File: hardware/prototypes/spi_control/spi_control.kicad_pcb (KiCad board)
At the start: 4 copper layers, 66.9 x 43.2 mm, 87 parts, among them J1 USB_B_Micro, J39 Versa_1, J40 Versa_2, U1 ST1L08SPU33R, U2 MCP2210-I_MQ, U3 ADAR7251, U4 BGT24_Module, Y1 12MHZ, Y2 40MHz

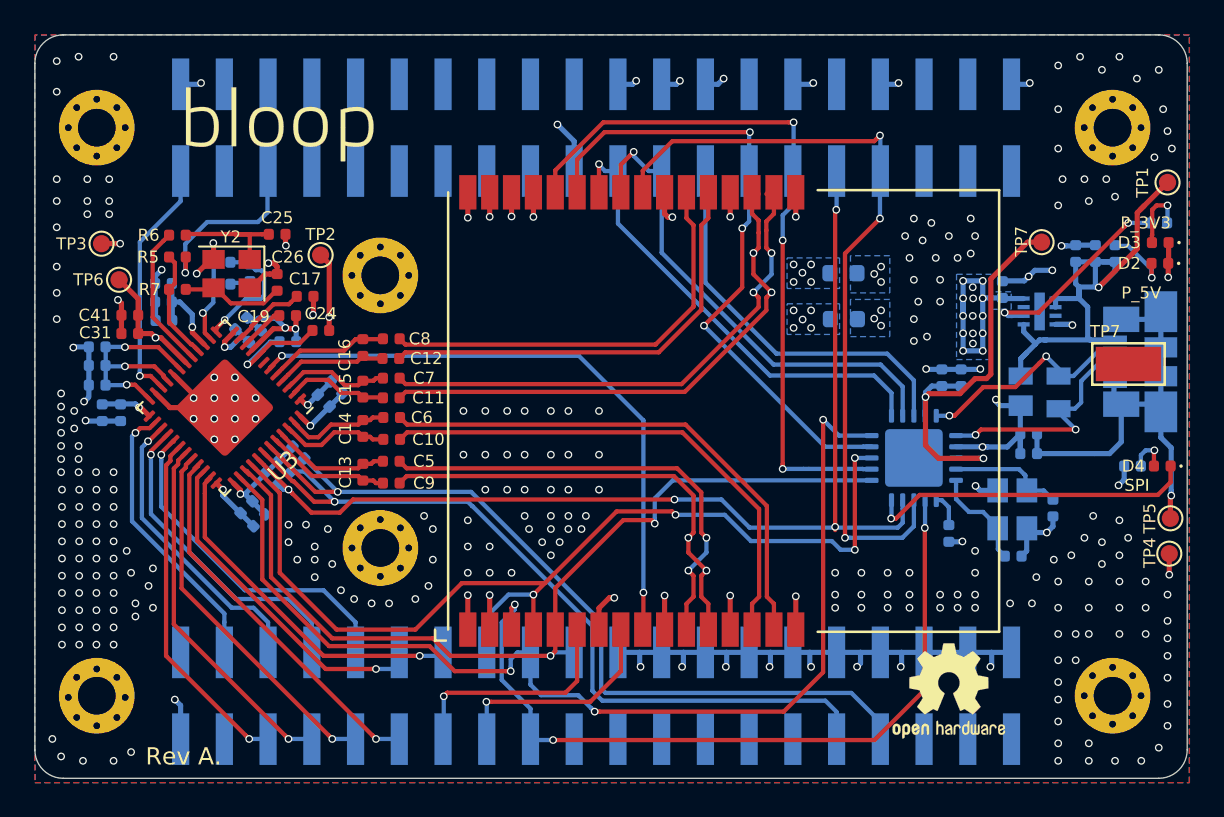
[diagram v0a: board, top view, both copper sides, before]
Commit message: Moved keystone to satisfy Leo.
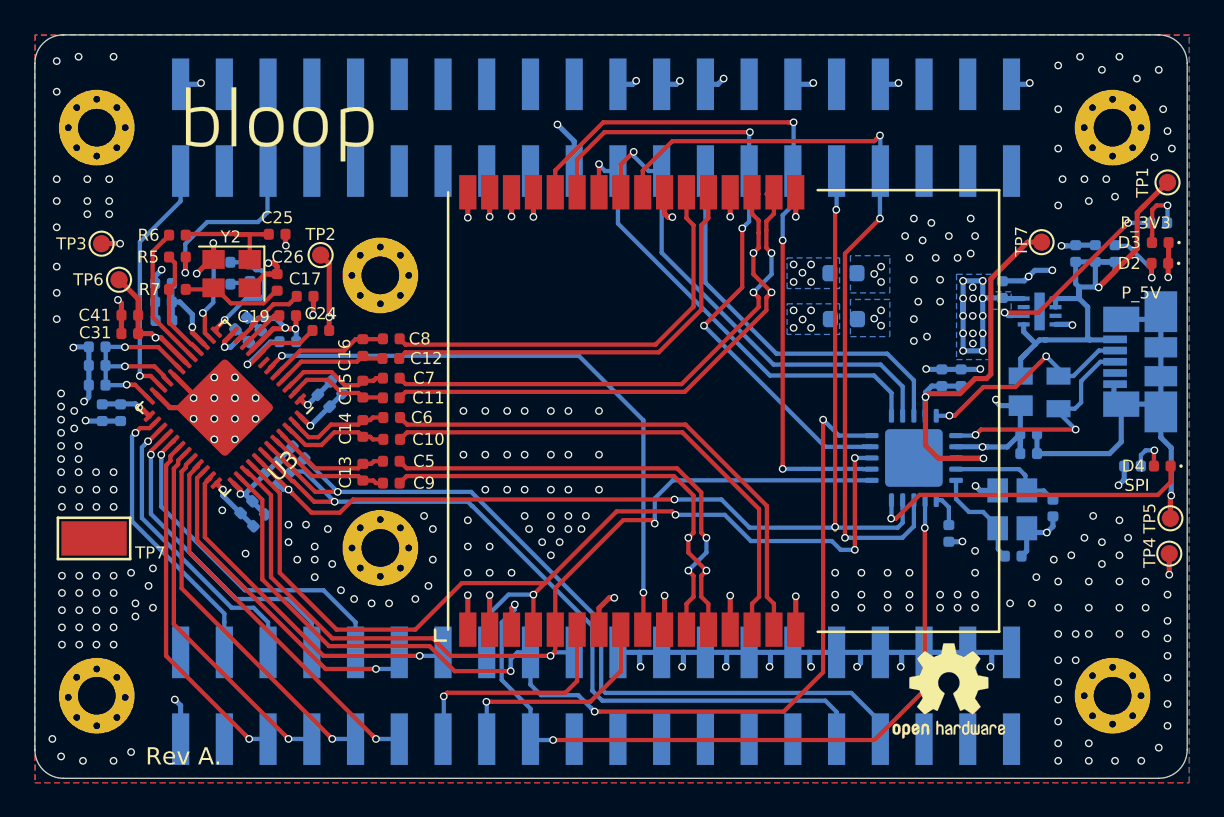
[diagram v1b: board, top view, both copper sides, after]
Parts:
- moved TP7 60.9 mm to (116.7, 114.3)
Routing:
- net GND: vias 261 -> 250
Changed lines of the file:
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@@
     (thickness 1.6)
     (drawings 15)
-    (tracks 1359)
+    (tracks 1348)
     (zones 0)
     (modules 87)
@@
   )
   (module TestPoint:TestPoint_Keystone_5019_Minature (layer F.Cu)
-    (at 176.80178 104.20604 180)
+    (at 116.72062 114.3381 180)
     (descr "SMT Test Point- Micro Miniature 5019, http://www.keyelco.com/product-pdf.cfm?p=1357")
     (tags "Test Point")
     (attr smd)
-    (fp_text reference TP7 (at 1.35382 1.88722) (layer F.SilkS)
+    (fp_text reference TP7 (at -3.27152 -0.84074) (layer F.SilkS)
       (effects (font (size 0.7 0.7) (thickness 0.15)))
     )
@@
       (rotate (xyz 0 0 0))
     )
+    (model ../../lib/3d/5019--3DModel-STEP-56544.STEP
+      (offset (xyz 0 0 1.1))
+      (scale (xyz 1 1 1))
+      (rotate (xyz -90 0 0))
+    )
   )
   (module Symbol:OSHW-Logo2_7.3x6mm_SilkScreen (layer F.Cu)
@@
   (via (at 116.8588 112.506) (size 0.45) (drill 0.3) (layers F.Cu B.Cu) (net 1))
   (via (at 117.8588 112.506) (size 0.45) (drill 0.3) (layers F.Cu B.Cu) (net 1))
-  (via (at 114.8588 113.506) (size 0.45) (drill 0.3) (layers F.Cu B.Cu) (net 1))
-  (via (at 115.8588 113.506) (size 0.45) (drill 0.3) (layers F.Cu B.Cu) (net 1))
-  (via (at 116.8588 113.506) (size 0.45) (drill 0.3) (layers F.Cu B.Cu) (net 1))
-  (via (at 117.8588 113.506) (size 0.45) (drill 0.3) (layers F.Cu B.Cu) (net 1))
-  (via (at 114.8588 114.506) (size 0.45) (drill 0.3) (layers F.Cu B.Cu) (net 1))
-  (via (at 115.8588 114.506) (size 0.45) (drill 0.3) (layers F.Cu B.Cu) (net 1))
-  (via (at 116.8588 114.506) (size 0.45) (drill 0.3) (layers F.Cu B.Cu) (net 1))
-  (via (at 117.8588 114.506) (size 0.45) (drill 0.3) (layers F.Cu B.Cu) (net 1))
-  (via (at 114.8588 115.506) (size 0.45) (drill 0.3) (layers F.Cu B.Cu) (net 1))
-  (via (at 115.8588 115.506) (size 0.45) (drill 0.3) (layers F.Cu B.Cu) (net 1))
-  (via (at 116.8588 115.506) (size 0.45) (drill 0.3) (layers F.Cu B.Cu) (net 1))
-  (via (at 117.8588 115.506) (size 0.45) (drill 0.3) (layers F.Cu B.Cu) (net 1))
   (via (at 114.8588 116.506) (size 0.45) (drill 0.3) (layers F.Cu B.Cu) (net 1))
   (via (at 115.8588 116.506) (size 0.45) (drill 0.3) (layers F.Cu B.Cu) (net 1))
@@
   (via (at 130.302 113.792) (size 0.45) (drill 0.3) (layers F.Cu B.Cu) (net 1))
   (via (at 129.54 115.57) (size 0.45) (drill 0.3) (layers F.Cu B.Cu) (net 1))
-  (via (at 118.618 115.062) (size 0.45) (drill 0.3) (layers F.Cu B.Cu) (net 1))
   (via (at 120.142 116.078) (size 0.45) (drill 0.3) (layers F.Cu B.Cu) (net 1))
   (via (at 118.872 116.332) (size 0.45) (drill 0.3) (layers F.Cu B.Cu) (net 1))
@@
   (via (at 176.276 86.36) (size 0.45) (drill 0.3) (layers F.Cu B.Cu) (net 1))
   (via (at 173.99 86.36) (size 0.45) (drill 0.3) (layers F.Cu B.Cu) (net 1))
+  (via (at 124.1679 112.70488) (size 0.45) (drill 0.3) (layers F.Cu B.Cu) (net 1))
+  (via (at 125.52172 115.21948) (size 0.45) (drill 0.3) (layers F.Cu B.Cu) (net 1))
   (segment (start 175.9585 106.4895) (end 175.9585 105.3465) (width 0.3) (layer B.Cu) (net 2))
   (segment (start 171.4905 109.4105) (end 171.4905 108.2675) (width 0.3) (layer B.Cu) (net 2))

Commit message: Resolve 4, 11, 16, 18, and 25 from #24 and includes misc. improvements
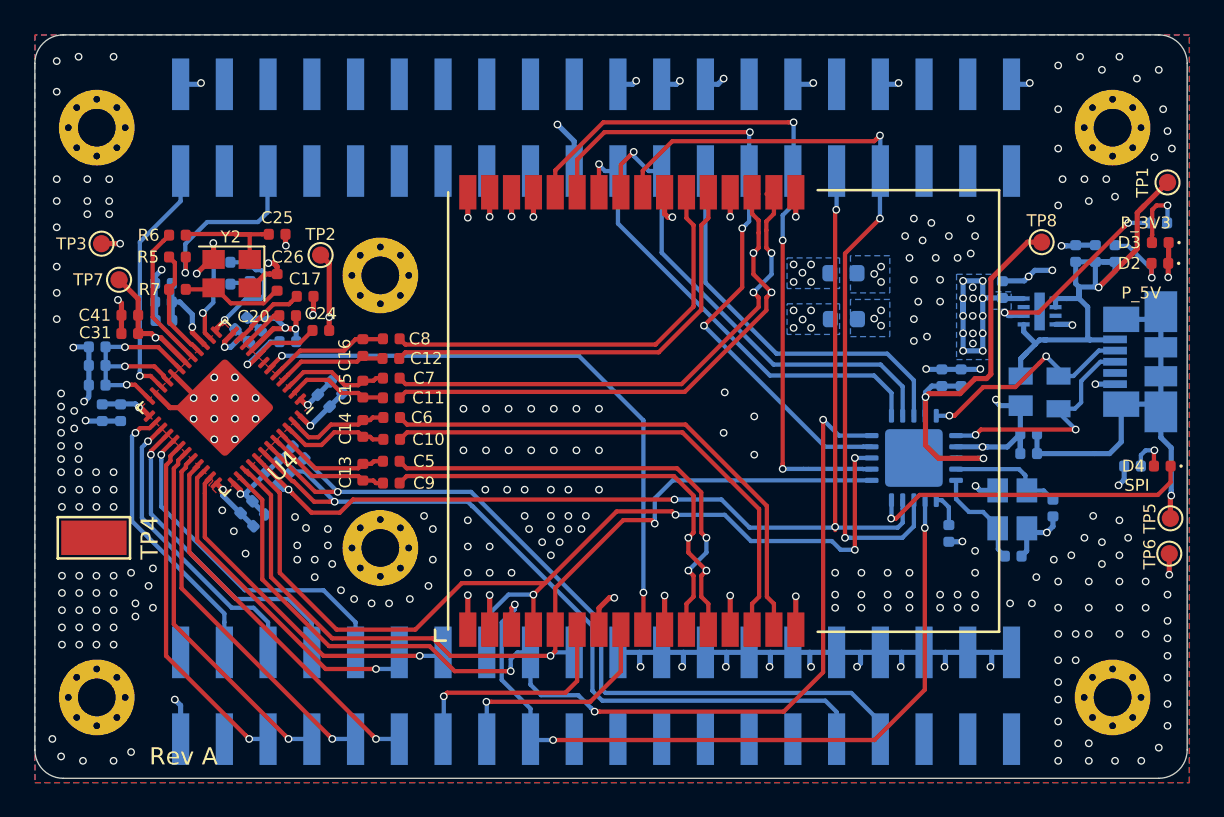
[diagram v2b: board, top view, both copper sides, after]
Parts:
- removed REF**: OSHW-Logo2_7.3x6mm_SilkScreen, Symbol:OSHW-Logo2_7.3x6mm_SilkScreen
- removed the TP7 at (116.7, 114.3)
- removed ~: LOGO, bloop:bloop_logo_text_silkandcopper
- added TP4: TestPoint, TestPoint:TestPoint_Keystone_5019_Minature, F.Cu at (116.7, 114.3)
- C10, C11, C12, C13, C14, C15, C16, C5, C6, C7, C8, C9: value C -> TBD
- H1, H2, H3, H4, H5, H6: value MountingHole_2.2mm_M2_Pad_Via -> MNT_HOLE
- moved H3 0.10 mm to (175.9, 123.6)
- renumbered C21 to C18, C18 to C19, C19 to C20, C20 to C21, FB2 to FB1, FB1 to FB2, J40 to J2, J39 to J3, TP4 to TP6, TP6 to TP7, TP7 to TP8, U4 to U1, U1 to U2, U2 to U3, U3 to U4
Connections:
- J1 pad 5: GNDREF -> GND
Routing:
- net GND: track 97.6 -> 98.7 mm, vias 250 -> 256
- net GNDREF: track 27.0 -> 25.8 mm
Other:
- board text added: "Rev A"
- board text removed: "Rev A."

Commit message: Resolve 9 from #24; added some vias to layout and moved a few tracks
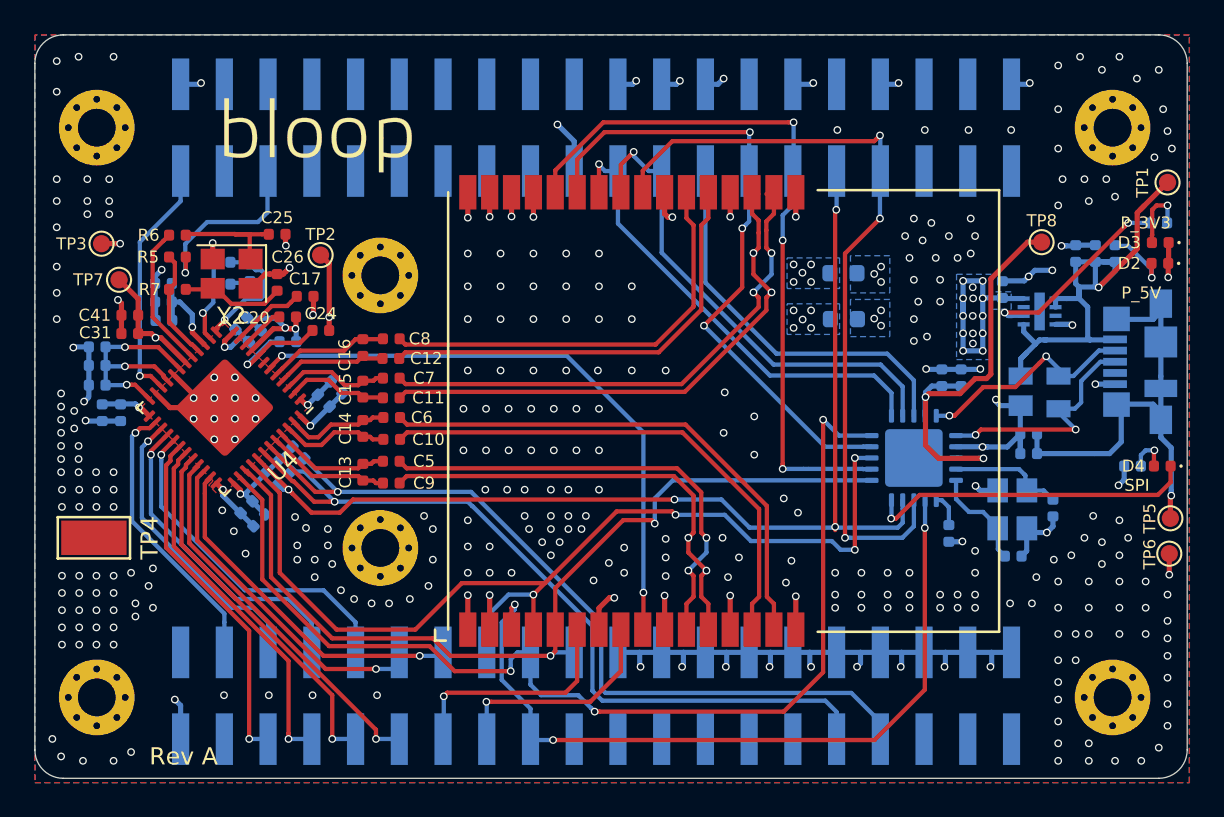
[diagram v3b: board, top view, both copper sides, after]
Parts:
- added ~: LOGO, bloop:bloop_logo_text_silkandcopper, F.Cu at (129.7, 91.1)
- Y2: footprint Oscillator:Oscillator_SMD_Abracon_ASE-4Pin_3.2x2.5mm -> Crystal:Crystal_SMD_Abracon_ABM8G-4Pin_3.2x2.5mm
- moved C20 0.08 mm to (128.0, 101.5)
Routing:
- net GND: track 98.7 -> 97.4 mm, vias 256 -> 289
- net GNDA: track 40.1 -> 40.0 mm, vias 52 -> 64
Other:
- rule trace_min: 0.2 -> 0.0889
- rule via_min_drill: 0.3 -> 0.2

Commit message: Finalize BOM, finish schematic annotations, re-generate gerbers. Close #24
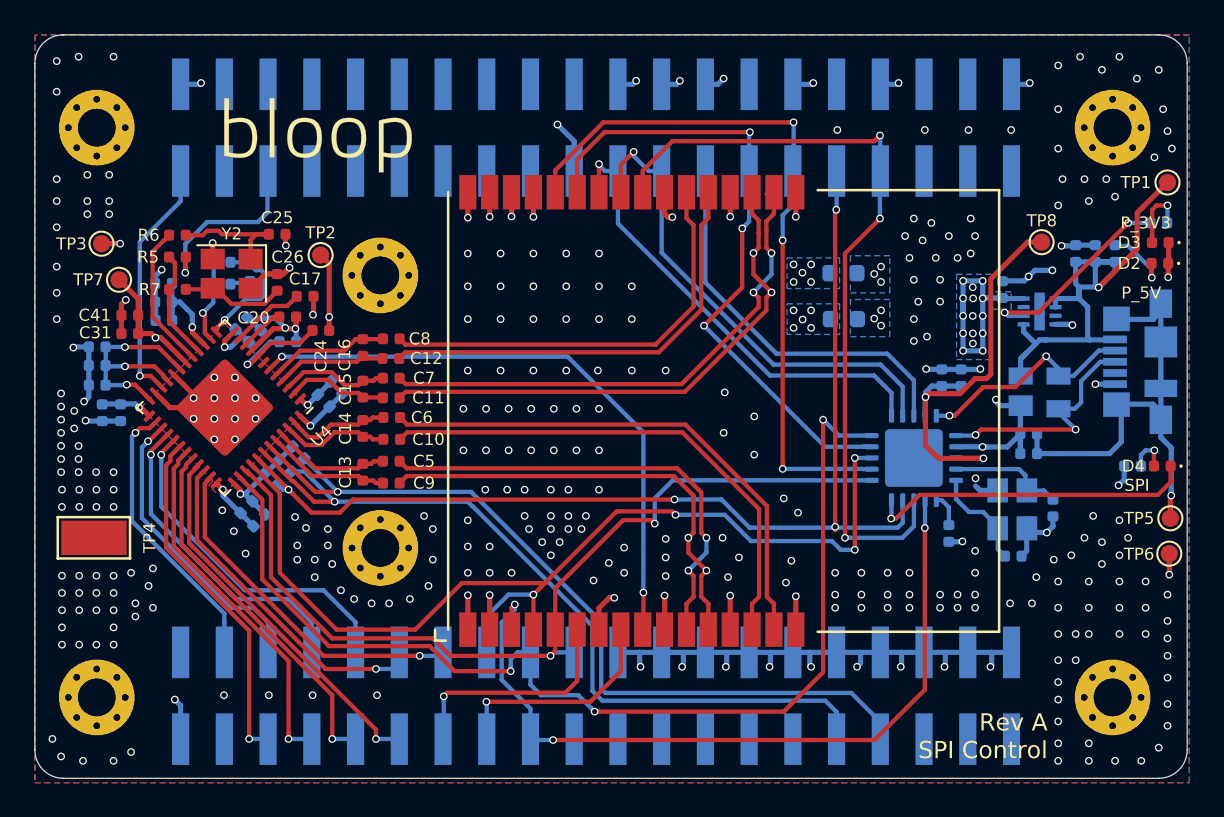
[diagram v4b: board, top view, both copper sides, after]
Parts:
- D2: value GREEN_LED -> GRN
- FB1, FB2: value Ferrite_Bead -> 1k
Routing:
- net GND: vias 289 -> 287
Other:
- board text added: "Rev A SPI Control"
- board text added: "→J39"
- board text added: "→J40"
- board text removed: "Rev A"
